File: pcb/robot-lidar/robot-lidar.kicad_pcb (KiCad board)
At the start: 2 copper layers, 45 parts, among them J1 Conn_ARM_SWD_TagConnect_TC2030, J2 YLIDAR X4, J3 Jack-DC, J4 Conn_02x03_Odd_Even, J5 Conn_01x02, J6 Conn_01x02, J7 Conn_01x02, J8 Conn_01x02, SW1 SW_SPST, U1 STM32F429VETx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

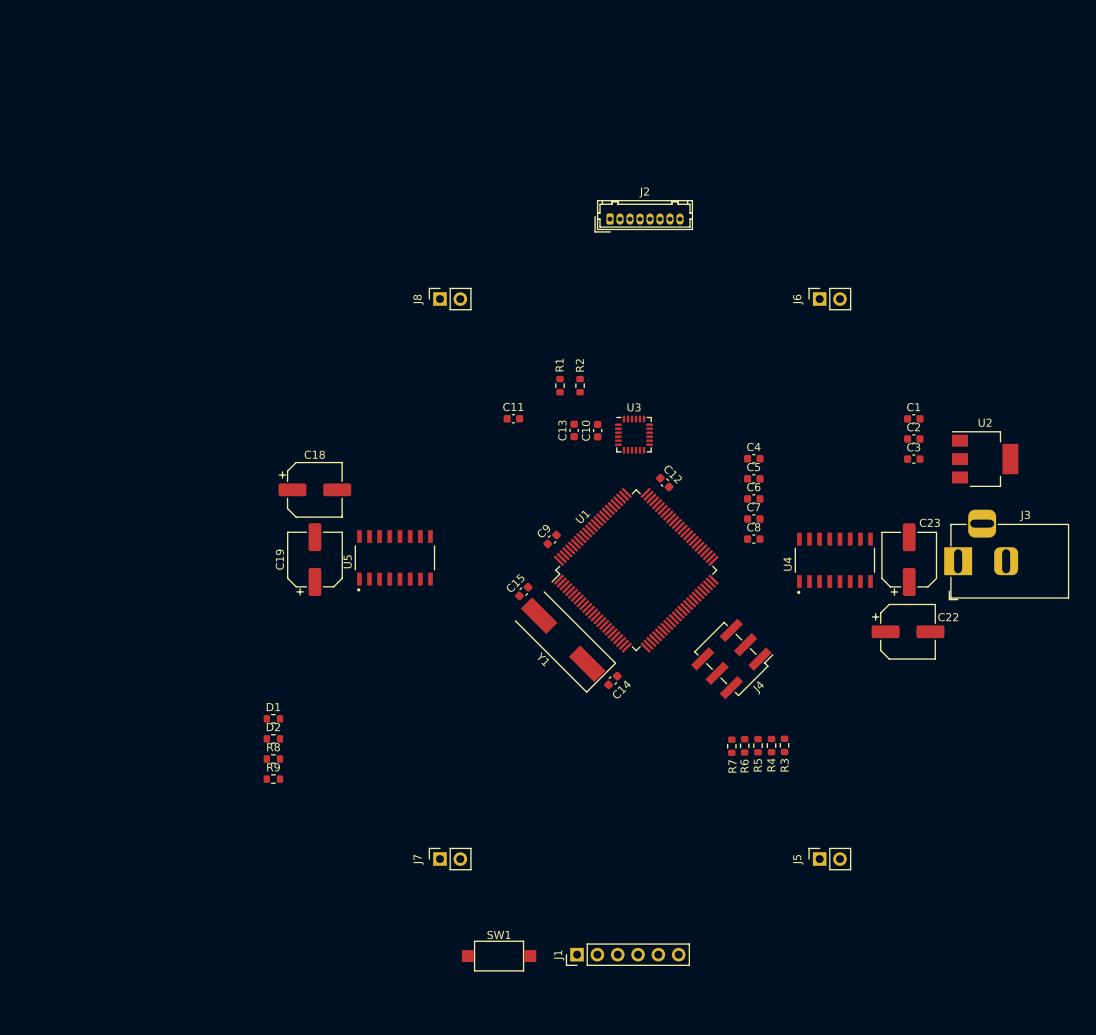
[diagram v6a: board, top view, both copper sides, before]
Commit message: wiring lidar
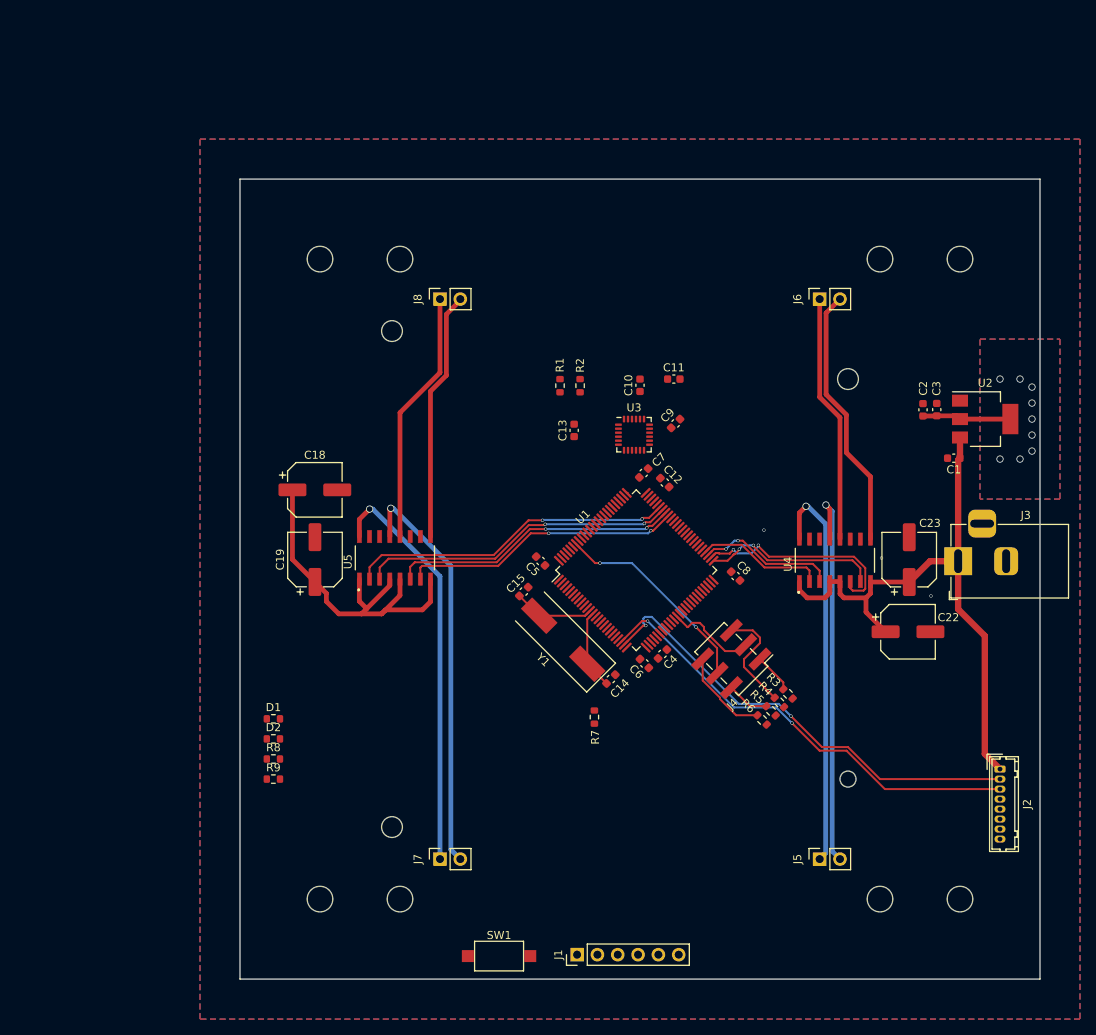
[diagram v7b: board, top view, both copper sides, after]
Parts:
- moved J2 84.3 mm to (145.0, 123.8), turned to -90 degrees
- moved C5 28.6 mm to (87.6, 97.7), turned to 135 degrees
- moved C4 26.9 mm to (102.8, 109.4), turned to -135 degrees
- moved C6 24.7 mm to (100.5, 110.5), turned to 135 degrees
- moved C9 21.2 mm to (104.5, 80.5)
- moved C11 20.7 mm to (104.2, 75.0)
- moved R7 17.6 mm to (94.3, 117.2)
- moved C7 14.9 mm to (100.5, 86.7), turned to -135 degrees
- moved C10 7.76 mm to (100.0, 75.8)
- moved C1 7.00 mm to (139.2, 84.9), turned to 180 degrees
- moved C3 6.82 mm to (137.1, 78.8), turned to 90 degrees
- moved R3 6.45 mm to (118.5, 114.3), turned to 135 degrees
- moved R4 5.49 mm to (117.4, 115.4), turned to -45 degrees
- moved C8 5.16 mm to (111.9, 99.6), turned to -45 degrees
- moved U2 5.00 mm to (143.2, 80.0)
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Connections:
- C12 pad 1: Net-(U1-VDDA) -> +3V3
- C13 pad 1: Net-(U1-VDDA) -> +3V3
- C2 pad 1: 3.3V -> +3V3
- C3 pad 1: 3.3V -> +3V3
- C4 pad 1: Net-(U1-VDDA) -> +3V3
- C5 pad 1: Net-(U1-VDDA) -> +3V3
- C6 pad 1: Net-(U1-VDDA) -> +3V3
- C7 pad 1: Net-(U1-VDDA) -> +3V3
- C8 pad 1: Net-(U1-VDDA) -> +3V3
- J2 pad 2: LIDAR_TX -> UART4_RX
- J2 pad 3: LIDAR_RX -> UART4_TX
- U1 pad 100: Net-(U1-VDDA) -> +3V3
- U1 pad 11: Net-(U1-VDDA) -> +3V3
- U1 pad 19: Net-(U1-VDDA) -> +3V3
- U1 pad 22: Net-(U1-VDDA) -> +3V3
- U1 pad 23: Net-(D1-A) -> UART4_TX
- U1 pad 24: Net-(D2-A) -> UART4_RX
- U1 pad 28: Net-(U1-VDDA) -> +3V3
- U1 pad 31: unconnected-(U1-PA6-Pad31) -> Net-(D1-A)
- U1 pad 32: unconnected-(U1-PA7-Pad32) -> Net-(D2-A)
- U1 pad 50: Net-(U1-VDDA) -> +3V3
- U1 pad 51: unconnected-(U1-PB12-Pad51) -> MOTOR_2_B
- U1 pad 52: unconnected-(U1-PB13-Pad52) -> MOTOR_2_A
- U1 pad 53: unconnected-(U1-PB14-Pad53) -> MOTOR_1_B
- U1 pad 54: unconnected-(U1-PB15-Pad54) -> MOTOR_1_A
- U1 pad 71: MOTOR_2_B -> unconnected-(U1-PA12-Pad71)
- U1 pad 72: MOTOR_2_A -> PA13-SWDIO
- U1 pad 75: Net-(U1-VDDA) -> +3V3
- U1 pad 76: MOTOR_1_B -> PA14-SWCLK
- U1 pad 77: MOTOR_1_A -> unconnected-(U1-PA15-Pad77)
- U1 pad 89: unconnected-(U1-PB3-Pad89) -> PB3-SWO
- U2 pad 2: 3.3V -> +3V3
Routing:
- net +5V: track 0.00 -> 124.5 mm
- net UART4_RX: track 0.00 -> 57.8 mm, vias 0 -> 2
- net UART4_TX: track 0.00 -> 57.1 mm, vias 0 -> 2
- net Net-(J7-Pin_1): track 0.00 -> 51.6 mm, vias 0 -> 1
- net Net-(J7-Pin_2): track 0.00 -> 51.2 mm, vias 0 -> 1
- net Net-(J5-Pin_1): track 0.00 -> 50.0 mm, vias 0 -> 1
- net Net-(J5-Pin_2): track 0.00 -> 49.5 mm, vias 0 -> 1
- net MOTOR_3_A: track 0.00 -> 40.9 mm, vias 0 -> 2
- net MOTOR_3_B: track 0.00 -> 39.8 mm, vias 0 -> 2
- net MOTOR_4_A: track 0.00 -> 36.2 mm, vias 0 -> 2
- net MOTOR_4_B: track 0.00 -> 35.1 mm, vias 0 -> 2
- net Net-(J6-Pin_2): track 0.00 -> 33.0 mm
- net Net-(J8-Pin_1): track 0.00 -> 31.8 mm
- net Net-(J8-Pin_2): track 0.00 -> 31.2 mm
- net Net-(J6-Pin_1): track 0.00 -> 31.1 mm
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- added copper zone on B.Cu, net +3V3
- added copper zone on F.Cu, net +3V3
- added copper zone on B.Cu, net GND
- added copper zone on F.Cu, net GND
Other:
- board outline added: 100 x 100 mm

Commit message: wiring mcp6500
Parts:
- added R10: 10K, Resistor_SMD:R_0603_1608Metric, F.Cu at (139.1, 131.7)
- added R11: 10K, Resistor_SMD:R_0603_1608Metric, F.Cu at (139.1, 128.5)
- added R12: 10K, Resistor_SMD:R_0603_1608Metric, F.Cu at (139.1, 130.1)
- moved R9 75.9 mm to (126.7, 147.5), turned to 90 degrees
- moved D2 74.7 mm to (123.6, 147.5), turned to 90 degrees
- moved D1 72.7 mm to (120.4, 147.4), turned to 90 degrees
- moved R8 68.3 mm to (117.8, 147.5), turned to 90 degrees
- moved C10 11.8 mm to (96.1, 86.9), turned to 180 degrees
- moved C11 4.76 mm to (100.8, 78.3)
- moved R1 4.19 mm to (94.2, 75.8)
- moved C13 3.22 mm to (94.9, 82.3)
- moved C9 2.20 mm to (103.5, 82.5), turned to -90 degrees
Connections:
- U1 pad 15: unconnected-(U1-PC0-Pad15) -> M_SCTR
- U1 pad 16: unconnected-(U1-PC1-Pad16) -> DEV_EN
- U1 pad 17: unconnected-(U1-PC2-Pad17) -> M_EN
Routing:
- net +3V3: track 11.1 -> 221.5 mm, vias 9 -> 13
- net +5V: track 124.5 -> 259.7 mm, vias 0 -> 2
- net Net-(D1-A): track 0.00 -> 74.7 mm, vias 0 -> 2
- net M_EN: track 0.00 -> 65.3 mm, vias 0 -> 2
- net DEV_EN: track 0.00 -> 65.1 mm, vias 0 -> 2
- net PA13-SWDIO: track 0.00 -> 64.5 mm, vias 0 -> 2
- net PA14-SWCLK: track 0.13 -> 62.9 mm, vias 0 -> 2
- net M_SCTR: track 0.00 -> 62.4 mm
- net Net-(D2-A): track 0.00 -> 58.7 mm, vias 0 -> 2
- net RESET: track 0.00 -> 57.7 mm, vias 0 -> 2
- net PB3-SWO: track 0.00 -> 57.7 mm, vias 0 -> 1
- net I2C_SDA: track 0.00 -> 29.3 mm
- net I2C_SCL: track 0.00 -> 28.8 mm, vias 0 -> 2
- net GND: track 0.00 -> 17.5 mm, vias 3 -> 19
- net Net-(U3-REGOUT): track 0.00 -> 5.52 mm, vias 0 -> 2
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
